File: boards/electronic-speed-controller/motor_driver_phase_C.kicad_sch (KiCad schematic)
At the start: 18 parts, among them U2 MIC4605-2YM-TR, U3 SISHA14DN-T1-GE3, U4 SISHA14DN-T1-GE3, U5 INA180A3IDBVR

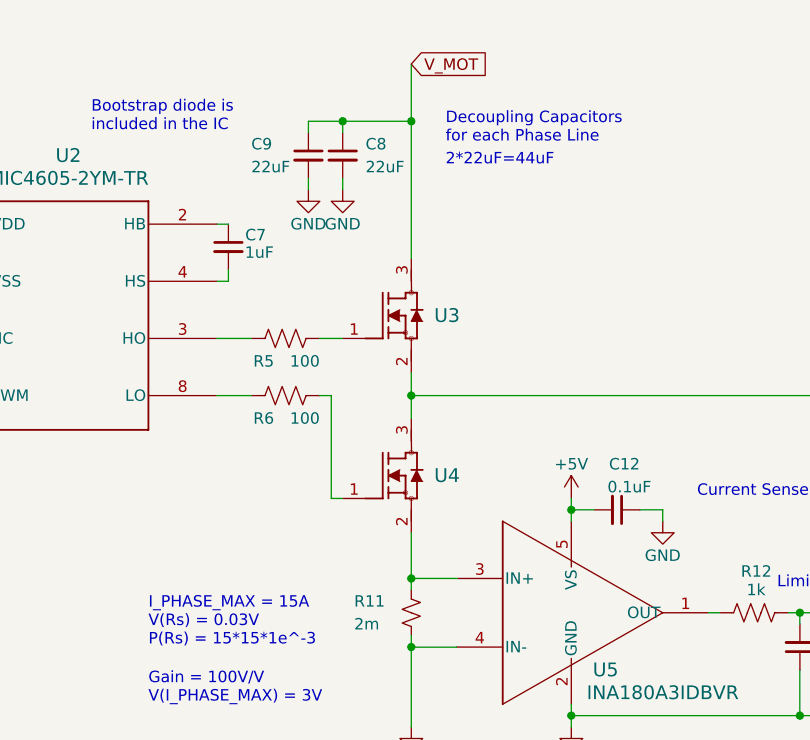
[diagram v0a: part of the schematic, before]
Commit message: updated MOSFETs
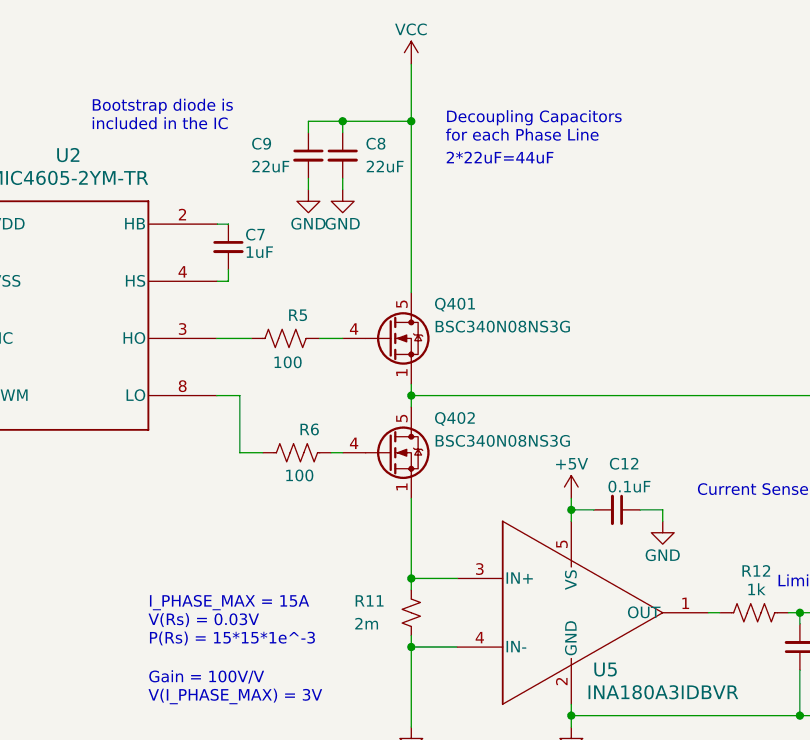
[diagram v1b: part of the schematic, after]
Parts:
- removed U3, U4: SISHA14DN-T1-GE3, MOSFET_3DN-T1-GE3_VIS, symbol N-Channel MOSFET:SISHA14DN-T1-GE3
- added Q401, Q402: BSC340N08NS3G, Package_TO_SOT_SMD:TDSON-8-1, symbol Transistor_FET:BSC340N08NS3G
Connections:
- net V_MOT is gone; now on net VCC: C8.1, C9.1
- net PHASE_C: now also Q401.1 (S), Q401.2 (S), Q401.3 (S), Q402.5 (D)
- net VCC: now also Q401.5 (D)
- net at R5.2: now also Q401.4 (G)
- net at R11.1, U5.3 (IN+): now also Q402.1 (S), Q402.2 (S), Q402.3 (S)
- net at R6.2: now also Q402.4 (G)
